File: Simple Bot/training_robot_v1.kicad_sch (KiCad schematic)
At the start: 14 parts, among them J1 Conn_01x08_Socket, J2 Conn_01x04_Socket, J3 Conn_01x04_Socket, M1 Motor_DC, M2 Motor_DC, M3 Motor_DC, M4 Motor_DC, SW1 SW_SPDT_312

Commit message: Fixed rats nest issue
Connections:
- net +12V: now also U1.1 (VCC), U1.3 (VCC), U2.1 (Vm), U3.1 (Vm); no longer U1. (VCC), U2. (Vm), U3. (Vm)
- net +3.3V: now also U2.2 (VCC), U3.2 (VCC); no longer U2. (Vm), U3. (Vm)
- net BL+: now also U3.7 (BO1); no longer U3. (Vm)
- net BL-: now also U3.6 (BO2); no longer U3. (Vm)
- net BR+: now also U2.7 (BO1); no longer U2. (Vm)
- net BR-: now also U2.6 (BO2); no longer U2. (Vm)
- net FL+: now also U3.4 (AO1); no longer U3. (Vm)
- net FL-: now also U3.5 (AO2); no longer U3. (Vm)
- net FR+: now also U2.4 (AO1); no longer U2. (Vm)
- net FR-: now also U2.5 (AO2); no longer U2. (Vm)
- net GND: now also U1.2 (GND), U1.4 (GND), U2.16 (GND), U2.3 (GND), U2.8 (GND), U3.16 (GND), U3.3 (GND), U3.8 (GND); no longer U1. (VCC), U2. (Vm), U3. (Vm)
- net STBY: now also U2.12 (STBY), U3.12 (STBY); no longer U2. (Vm), U3. (Vm)
- net at J1.3 (Pin_3): now also U2.15 (PWMB), U2.9 (PWMA); no longer U2. (Vm)
- net at J1.4 (Pin_4): now also U2.11 (AI1), U2.13 (BI1); no longer U2. (Vm)
- net at J1.5 (Pin_5): now also U2.10 (AI2), U2.14 (BI2); no longer U2. (Vm)
- net at J1.6 (Pin_6): now also U3.15 (PWMB), U3.9 (PWMA); no longer U3. (Vm)
- net at J1.7 (Pin_7): now also U3.11 (AI1), U3.13 (BI1); no longer U3. (Vm)
- net at J1.8 (Pin_8): now also U3.10 (AI2), U3.14 (BI2); no longer U3. (Vm)
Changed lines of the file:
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@@
 	(wire
 		(pts
-			(xy 134.62 111.76) (xy 137.16 111.76)
+			(xy 130.81 111.76) (xy 137.16 111.76)
+		)
+		(stroke
+			(width 0)
+			(type default)
+		)
+	)
+	(wire
+		(pts
+			(xy 133.35 121.92) (xy 137.16 121.92)
+		)
+		(stroke
+			(width 0)
+			(type default)
+		)
+	)
+	(wire
+		(pts
+			(xy 133.35 116.84) (xy 137.16 116.84)
+		)
+		(stroke
+			(width 0)
+			(type default)
+		)
+	)
+	(wire
+		(pts
+			(xy 133.35 148.59) (xy 137.16 148.59)
 		)
 		(stroke
@@
 	(wire
 		(pts
-			(xy 134.62 140.97) (xy 137.16 140.97)
+			(xy 132.08 140.97) (xy 137.16 140.97)
 		)
 		(stroke
@@
 	(wire
 		(pts
+			(xy 133.35 119.38) (xy 137.16 119.38)
+		)
+		(stroke
+			(width 0)
+			(type default)
+		)
+	)
+	(wire
+		(pts
 			(xy 67.31 92.71) (xy 74.93 92.71)
 		)
@@
 	(wire
 		(pts
+			(xy 133.35 151.13) (xy 137.16 151.13)
+		)
+		(stroke
+			(width 0)
+			(type default)
+		)
+	)
+	(wire
+		(pts
 			(xy 184.15 133.35) (xy 176.53 133.35)
 		)
@@
 	(wire
 		(pts
-			(xy 134.62 153.67) (xy 137.16 153.67)
+			(xy 132.08 153.67) (xy 137.16 153.67)
+		)
+		(stroke
+			(width 0)
+			(type default)
+		)
+	)
+	(wire
+		(pts
+			(xy 133.35 146.05) (xy 137.16 146.05)
 		)
 		(stroke
@@
 		(pts
 			(xy 134.62 124.46) (xy 137.16 124.46)
+		)
+		(stroke
+			(width 0)
+			(type default)
+		)
+	)
+	(wire
+		(pts
+			(xy 133.35 114.3) (xy 137.16 114.3)
+		)
+		(stroke
+			(width 0)
+			(type default)
+		)
+	)
+	(wire
+		(pts
+			(xy 133.35 143.51) (xy 137.16 143.51)
 		)
 		(stroke
@@
 	)
 	(label "FL-"
-		(at 137.16 146.05 0)
+		(at 133.35 146.05 0)
 		(fields_autoplaced yes)
 		(effects
@@
 	)
 	(label "BL+"
-		(at 137.16 151.13 0)
+		(at 133.35 151.13 0)
 		(fields_autoplaced yes)
 		(effects
@@
 	)
 	(label "BR-"
-		(at 137.16 119.38 0)
+		(at 133.35 119.38 0)
 		(fields_autoplaced yes)
 		(effects
@@
 	)
 	(label "FR-"
-		(at 137.16 116.84 0)
+		(at 133.35 116.84 0)
 		(fields_autoplaced yes)
 		(effects
@@
 	)
 	(label "BL-"
-		(at 137.16 148.59 0)
+		(at 133.35 148.59 0)
 		(fields_autoplaced yes)
 		(effects
@@
 	)
 	(label "BR+"
-		(at 137.16 121.92 0)
+		(at 133.35 121.92 0)
 		(fields_autoplaced yes)
 		(effects
@@
 	)
 	(label "FL+"
-		(at 137.16 143.51 0)
+		(at 133.35 143.51 0)
 		(fields_autoplaced yes)
 		(effects
@@
 	)
 	(label "FR+"
-		(at 137.16 114.3 0)
+		(at 133.35 114.3 0)
 		(fields_autoplaced yes)
 		(effects
@@
 			)
 		)
-		(pin ""
-		)
-		(pin ""
-		)
-		(pin ""
-		)
-		(pin ""
+		(pin "1"
+		)
+		(pin "2"
+		)
+		(pin "3"
+		)
+		(pin "4"
 		)
 		(instances
@@
 	)
 	(symbol
-		(lib_name "Breakout_tb6612FNG_1")
+		(lib_name "Breakout_tb6612FNG_2")
 		(lib_id "Custom_Lib:Breakout_tb6612FNG")
 		(at 148.59 102.87 0)
@@
 			)
 		)
-		(pin ""
-		)
-		(pin ""
-		)
-		(pin ""
-		)
-		(pin ""
-		)
-		(pin ""
-		)
-		(pin ""
-		)
-		(pin ""
-		)
-		(pin ""
-		)
-		(pin ""
-		)
-		(pin ""
-		)
-		(pin ""
-		)
-		(pin ""
-		)
-		(pin ""
-		)
-		(pin ""
-		)
-		(pin ""
-		)
-		(pin ""
+		(pin "12"
+		)
+		(pin "9"
+		)
+		(pin "8"
+		)
+		(pin "4"
+		)
+		(pin "5"
+		)
+		(pin "11"
+		)
+		(pin "15"
+		)
+		(pin "16"
+		)
+		(pin "6"
+		)
+		(pin "3"
+		)
+		(pin "14"
+		)
+		(pin "7"
+		)
+		(pin "13"
+		)
+		(pin "10"
+		)
+		(pin "2"
+		)
+		(pin "1"
 		)
 		(instances
@@
 	(symbol
 		(lib_id "power:GND")
-		(at 134.62 140.97 270)
+		(at 132.08 140.97 270)
 		(unit 1)
 		(exclude_from_sim no)
@@
 		(fields_autoplaced yes)
 		(property "Reference" "#PWR08"
-			(at 128.27 140.97 0)
+			(at 125.73 140.97 0)
 			(effects
 				(font
@@
 		)
 		(property "Value" "GND"
-			(at 130.81 140.9699 90)
+			(at 128.27 140.9699 90)
 			(effects
 				(font
@@
 		)
 		(property "Footprint" ""
-			(at 134.62 140.97 0)
+			(at 132.08 140.97 0)
 			(effects
 				(font
@@
 		)
 		(property "Datasheet" ""
-			(at 134.62 140.97 0)
+			(at 132.08 140.97 0)
 			(effects
 				(font
@@
 		)
 		(property "Description" "Power symbol creates a global label with name \"GND\" , ground"
-			(at 134.62 140.97 0)
+			(at 132.08 140.97 0)
 			(effects
 				(font
@@
 			)
 		)
-		(pin ""
-		)
-		(pin ""
-		)
-		(pin ""
-		)
-		(pin ""
-		)
-		(pin ""
-		)
-		(pin ""
-		)
-		(pin ""
-		)
-		(pin ""
-		)
-		(pin ""
-		)
-		(pin ""
-		)
-		(pin ""
-		)
-		(pin ""
-		)
-		(pin ""
-		)
-		(pin ""
-		)
-		(pin ""
-		)
-		(pin ""
+		(pin "4"
+		)
+		(pin "5"
+		)
+		(pin "13"
+		)
+		(pin "14"
+		)
+		(pin "7"
+		)
+		(pin "6"
+		)
+		(pin "8"
+		)
+		(pin "3"
+		)
+		(pin "16"
+		)
+		(pin "9"
+		)
+		(pin "15"
+		)
+		(pin "12"
+		)
+		(pin "2"
+		)
+		(pin "1"
+		)
+		(pin "11"
+		)
+		(pin "10"
 		)
 		(instances
@@
 	(symbol
 		(lib_id "power:GND")
-		(at 134.62 153.67 270)
+		(at 132.08 153.67 270)
 		(unit 1)
 		(exclude_from_sim no)
@@
 		(fields_autoplaced yes)
 		(property "Reference" "#PWR07"
-			(at 128.27 153.67 0)
+			(at 125.73 153.67 0)
 			(effects
 				(font
@@
 		)
 		(property "Value" "GND"
-			(at 130.81 153.6699 90)
+			(at 128.27 153.6699 90)
 			(effects
 				(font
@@
 		)
 		(property "Footprint" ""
-			(at 134.62 153.67 0)
+			(at 132.08 153.67 0)
 			(effects
 				(font
@@
 		)
 		(property "Datasheet" ""
-			(at 134.62 153.67 0)
+			(at 132.08 153.67 0)
 			(effects
 				(font
@@
 		)
 		(property "Description" "Power symbol creates a global label with name \"GND\" , ground"
-			(at 134.62 153.67 0)
+			(at 132.08 153.67 0)
 			(effects
 				(font
@@
 	(symbol
 		(lib_id "power:GND")
-		(at 134.62 111.76 270)
+		(at 130.81 111.76 270)
 		(unit 1)
 		(exclude_from_sim no)
@@
 		(dnp no)
 		(property "Reference" "#PWR011"
-			(at 128.27 111.76 0)
+			(at 124.46 111.76 0)
 			(effects
 				(font
@@
 		)
 		(property "Value" "GND"
-			(at 131.064 111.76 90)
+			(at 127.254 111.76 90)
 			(effects
 				(font
@@
 		)
 		(property "Footprint" ""
-			(at 134.62 111.76 0)
+			(at 130.81 111.76 0)
 			(effects
 				(font
@@
 		)
 		(property "Datasheet" ""
-			(at 134.62 111.76 0)
+			(at 130.81 111.76 0)
 			(effects
 				(font
@@
 		)
 		(property "Description" "Power symbol creates a global label with name \"GND\" , ground"
-			(at 134.62 111.76 0)
-			(effects
-				(font
+			(at 130.81 111.76 0)
+			(effects
+				(font

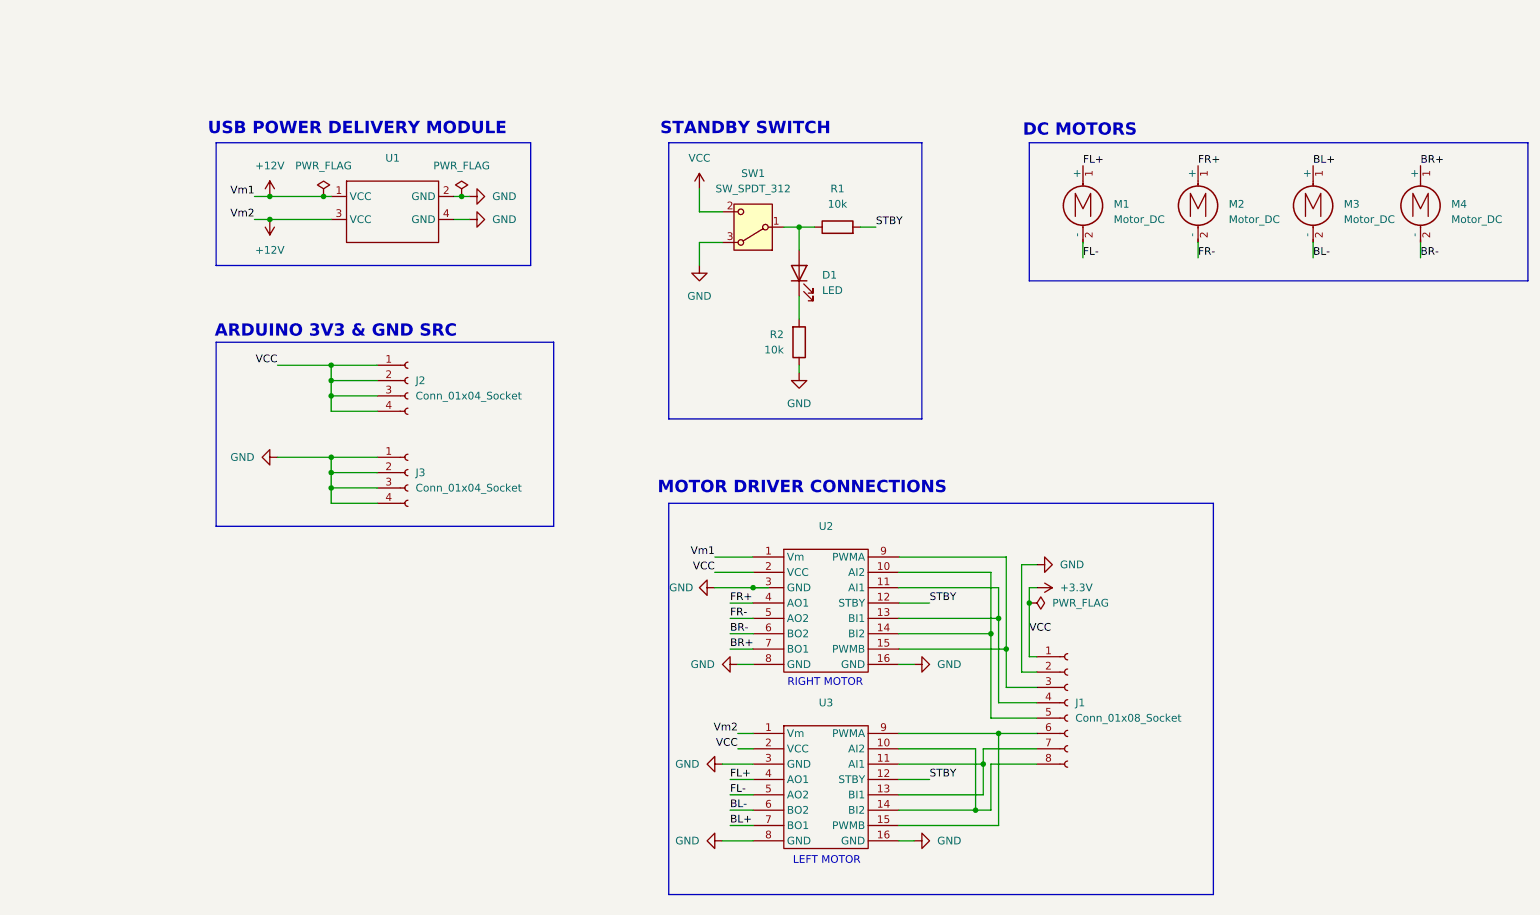
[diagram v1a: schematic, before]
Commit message: Removed schematic details
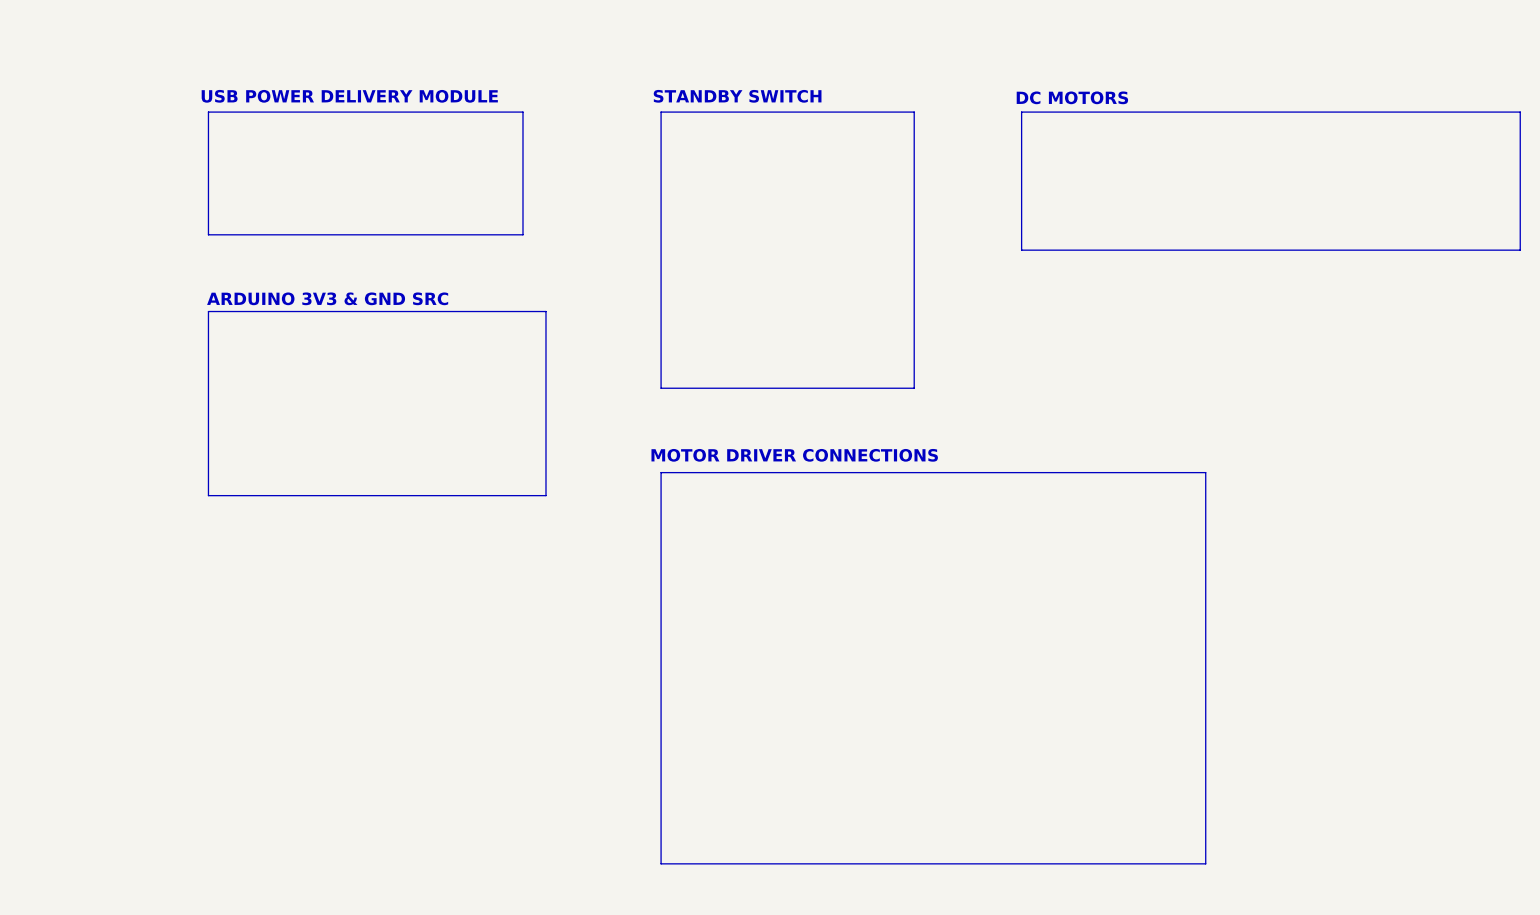
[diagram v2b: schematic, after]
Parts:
- removed D1: LED, LED_THT:LED_D3.0mm, symbol Device:LED
- removed J1: Conn_01x08_Socket, Connector_PinSocket_2.54mm:PinSocket_1x08_P2.54mm_Vertical, symbol Connector:Conn_01x08_Socket
- removed J2, J3: Conn_01x04_Socket, Connector_PinSocket_2.54mm:PinSocket_1x04_P2.54mm_Vertical, symbol Connector:Conn_01x04_Socket
- removed M1, M2, M3, M4: Motor_DC, TerminalBlock:TerminalBlock_Xinya_XY308-2.54-2P_1x02_P2.54mm_Horizontal, symbol Motor:Motor_DC
- removed R1, R2: 10k, Resistor_THT:R_Axial_DIN0204_L3.6mm_D1.6mm_P5.08mm_Horizontal, symbol Device:R
- removed SW1: SW_SPDT_312, Button_Switch_THT:SW_Slide_SPDT_Straight_CK_OS102011MS2Q, symbol Switch:SW_SPDT_312
- removed U1: ~, custom_lib:PD Module, symbol Custom_Lib:PD_Module
- removed U2, U3: ~, custom_lib:TB_breakout_motor_driver, symbol Custom_Lib:Breakout_tb6612FNG
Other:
- note removed: "LEFT MOTOR"
- note removed: "RIGHT MOTOR"

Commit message: replaced "simple" sch and pcb files with Josalin's
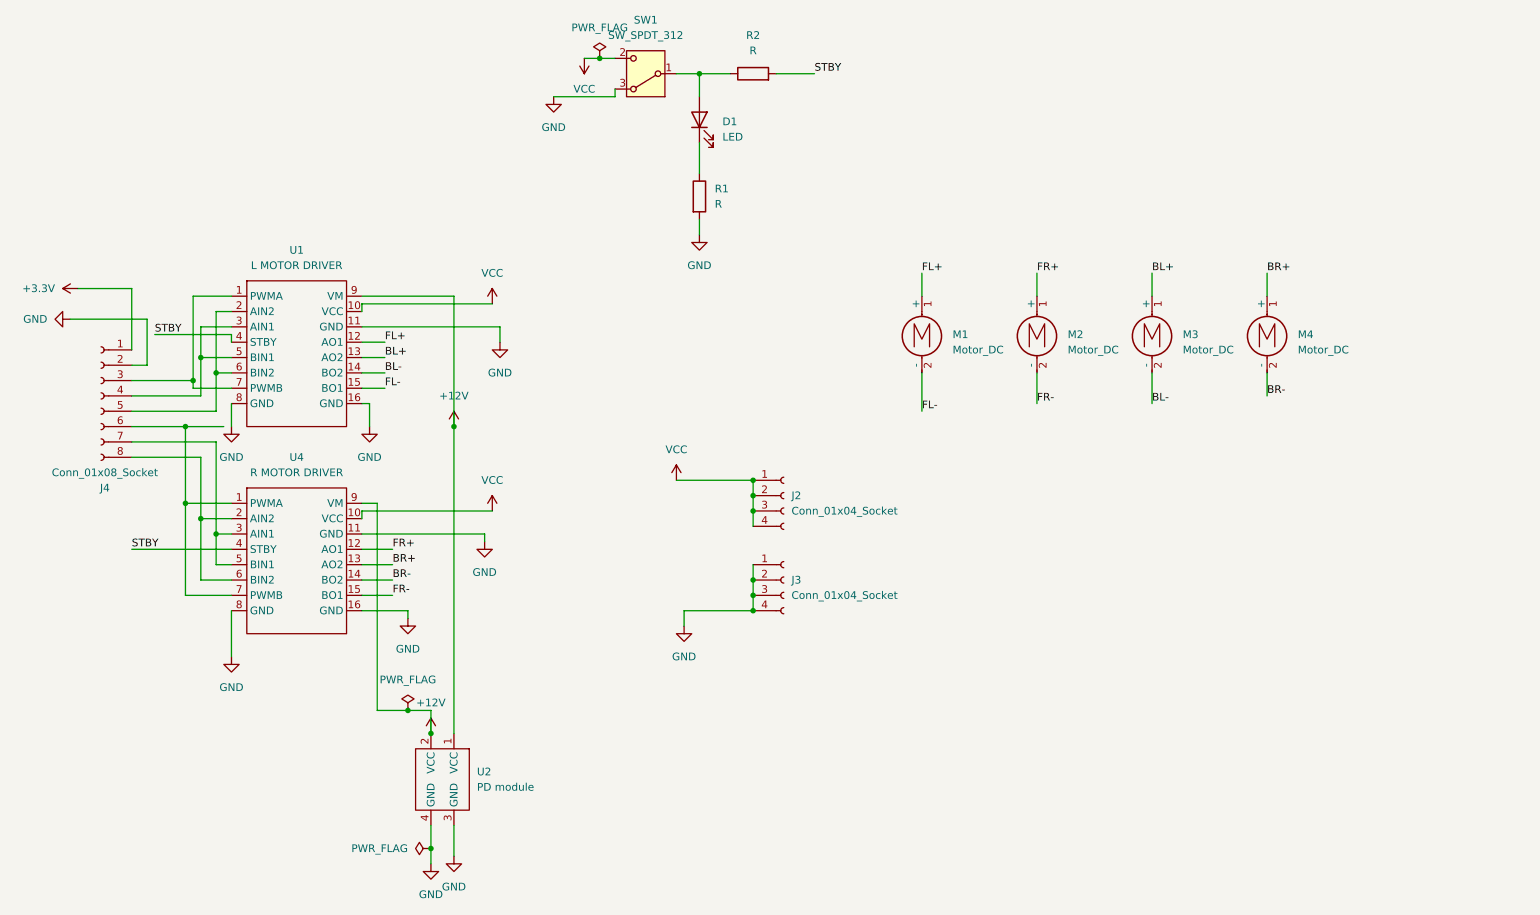
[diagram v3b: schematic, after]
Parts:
- added D1: LED, LED_THT:LED_D3.0mm, symbol Device:LED
- added J2, J3: Conn_01x04_Socket, Connector_PinSocket_2.54mm:PinSocket_1x04_P2.54mm_Vertical, symbol Connector:Conn_01x04_Socket
- added J4: Conn_01x08_Socket, Connector_PinSocket_2.54mm:PinSocket_1x08_P2.54mm_Vertical, symbol Connector:Conn_01x08_Socket
- added M1, M2, M3, M4: Motor_DC, TerminalBlock:TerminalBlock_Xinya_XY308-2.54-2P_1x02_P2.54mm_Horizontal, symbol Motor:Motor_DC
- added R1, R2: R, Resistor_THT:R_Axial_DIN0204_L3.6mm_D1.6mm_P5.08mm_Horizontal, symbol Device:R
- added SW1: SW_SPDT_312, Button_Switch_THT:SW_Slide_SPDT_Straight_CK_OS102011MS2Q, symbol Switch:SW_SPDT_312
- added U1: L MOTOR DRIVER, training-bot-footprint:TB_breakout_motor_driver, symbol trainingbot_board:Motor_Driver
- added U2: PD module, training-bot-footprint:PD Module, symbol trainingbot_board:USB_PD
- added U4: R MOTOR DRIVER, training-bot-footprint:TB_breakout_motor_driver, symbol trainingbot_board:Motor_Driver
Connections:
- new net: J4.3 (Pin_3), U1.1 (PWMA), U1.7 (PWMB)
- new net: J4.5 (Pin_5), U1.2 (AIN2), U1.6 (BIN2)
- new net: J4.4 (Pin_4), U1.3 (AIN1), U1.5 (BIN1)
- new net: J4.6 (Pin_6), U4.1 (PWMA), U4.7 (PWMB)
- new net: J4.8 (Pin_8), U4.2 (AIN2), U4.6 (BIN2)
- new net: J4.7 (Pin_7), U4.3 (AIN1), U4.5 (BIN1)
- new net: D1.1 (K), R1.1
- new net: D1.2 (A), R2.1, SW1.1 (B)
- new net +12V: U1.9 (VM), U2.1 (VCC), U2.2 (VCC), U4.9 (VM)
- new net +3.3V: J4.1 (Pin_1)
- new net BL+: M3.1 (+), U1.13 (AO2)
- new net BL-: M3.2 (-), U1.14 (BO2)
- new net BR+: M4.1 (+), U4.13 (AO2)
- new net BR-: M4.2 (-), U4.14 (BO2)
- new net FL+: M1.1 (+), U1.12 (AO1)
- new net FL-: M1.2 (-), U1.15 (BO1)
- new net FR+: M2.1 (+), U4.12 (AO1)
- new net FR-: M2.2 (-), U4.15 (BO1)
- new net GND: J3.1 (Pin_1), J3.2 (Pin_2), J3.3 (Pin_3), J3.4 (Pin_4), J4.2 (Pin_2), R1.2, SW1.3 (A), U1.11 (GND), U1.16 (GND), U1.8 (GND), U2.3 (GND), U2.4 (GND), U4.11 (GND), U4.16 (GND), U4.8 (GND)
- new net STBY: R2.2, U1.4 (STBY), U4.4 (STBY)
- new net VCC: J2.1 (Pin_1), J2.2 (Pin_2), J2.3 (Pin_3), J2.4 (Pin_4), SW1.2 (C), U1.10 (VCC), U4.10 (VCC)
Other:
- note removed: "ARDUINO 3V3 & GND SRC"
- note removed: "DC MOTORS"
- note removed: "MOTOR DRIVER CONNECTIONS"
- note removed: "STANDBY SWITCH"
- note removed: "USB POWER DELIVERY MODULE"
